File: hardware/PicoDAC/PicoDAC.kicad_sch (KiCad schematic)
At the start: 42 parts, among them CN1 PJ-327A 5JJ, U1 CS43131-CNZR, U2 XIAO-RP2350-DIP, U3 PCA9306DCUR, U4 SN74AXC4T245PWR, U5 XTPS7A2018, U6 TYPEC-955-ARP24, U7 74AHCT1G125GV

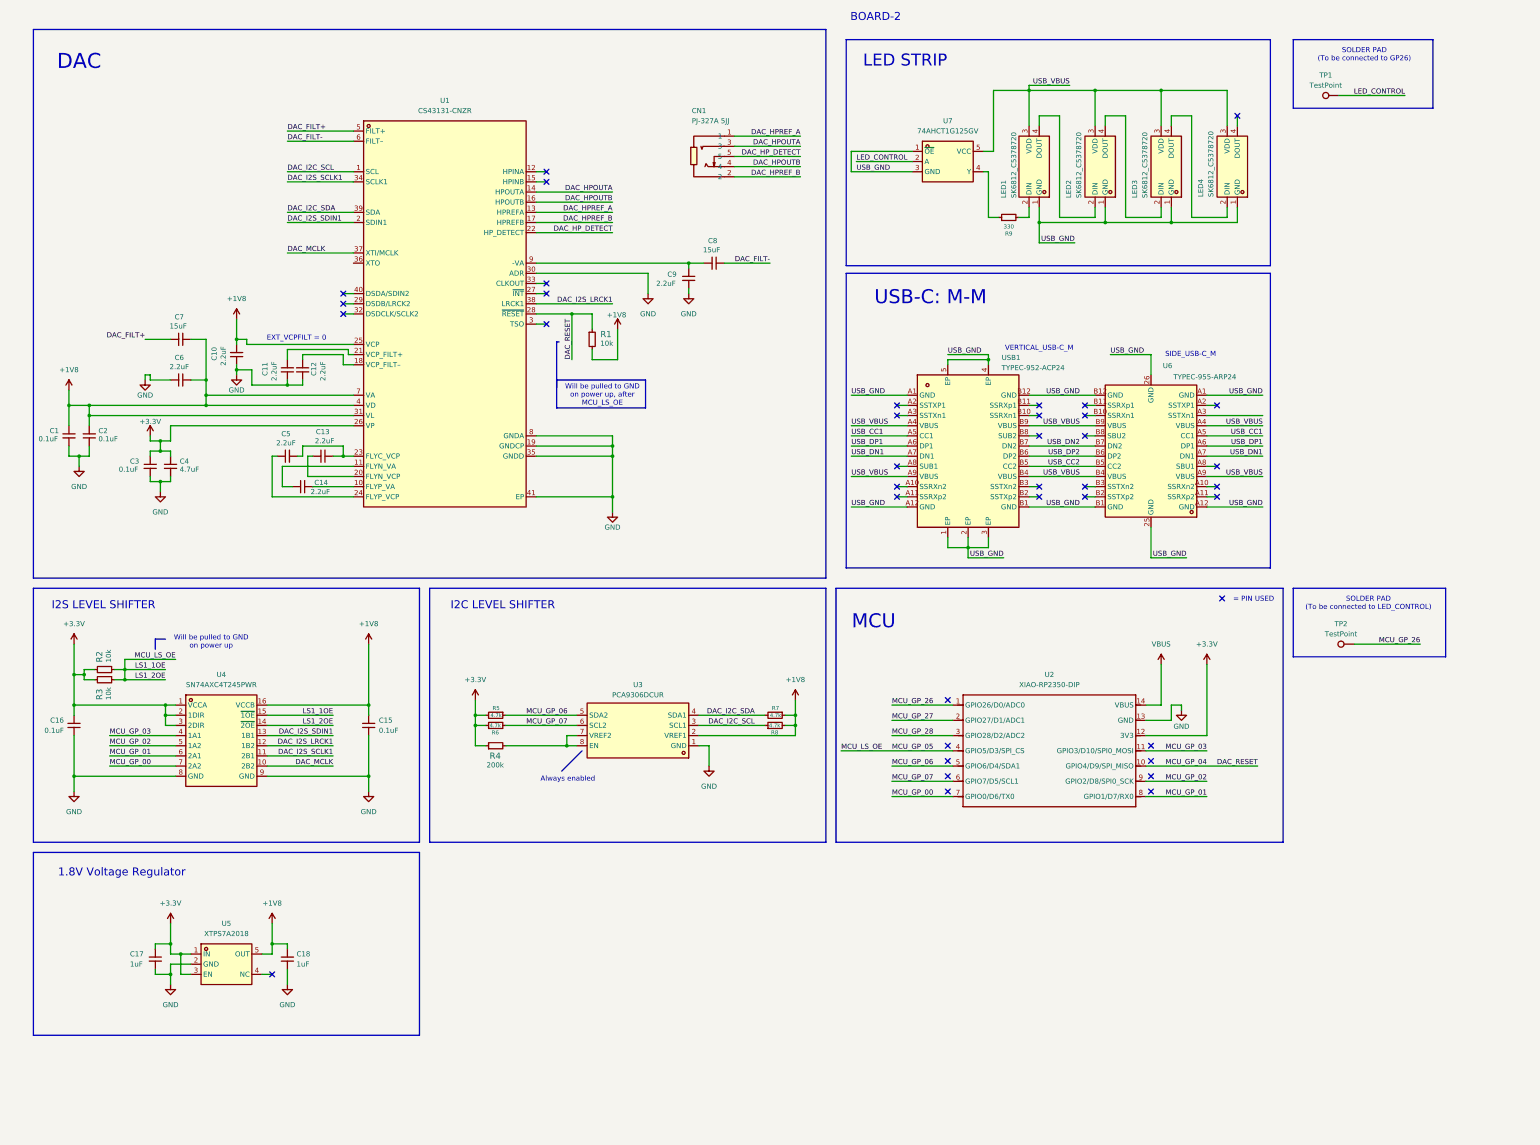
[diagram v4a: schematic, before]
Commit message: update LEDs position, misc changes to PCBs
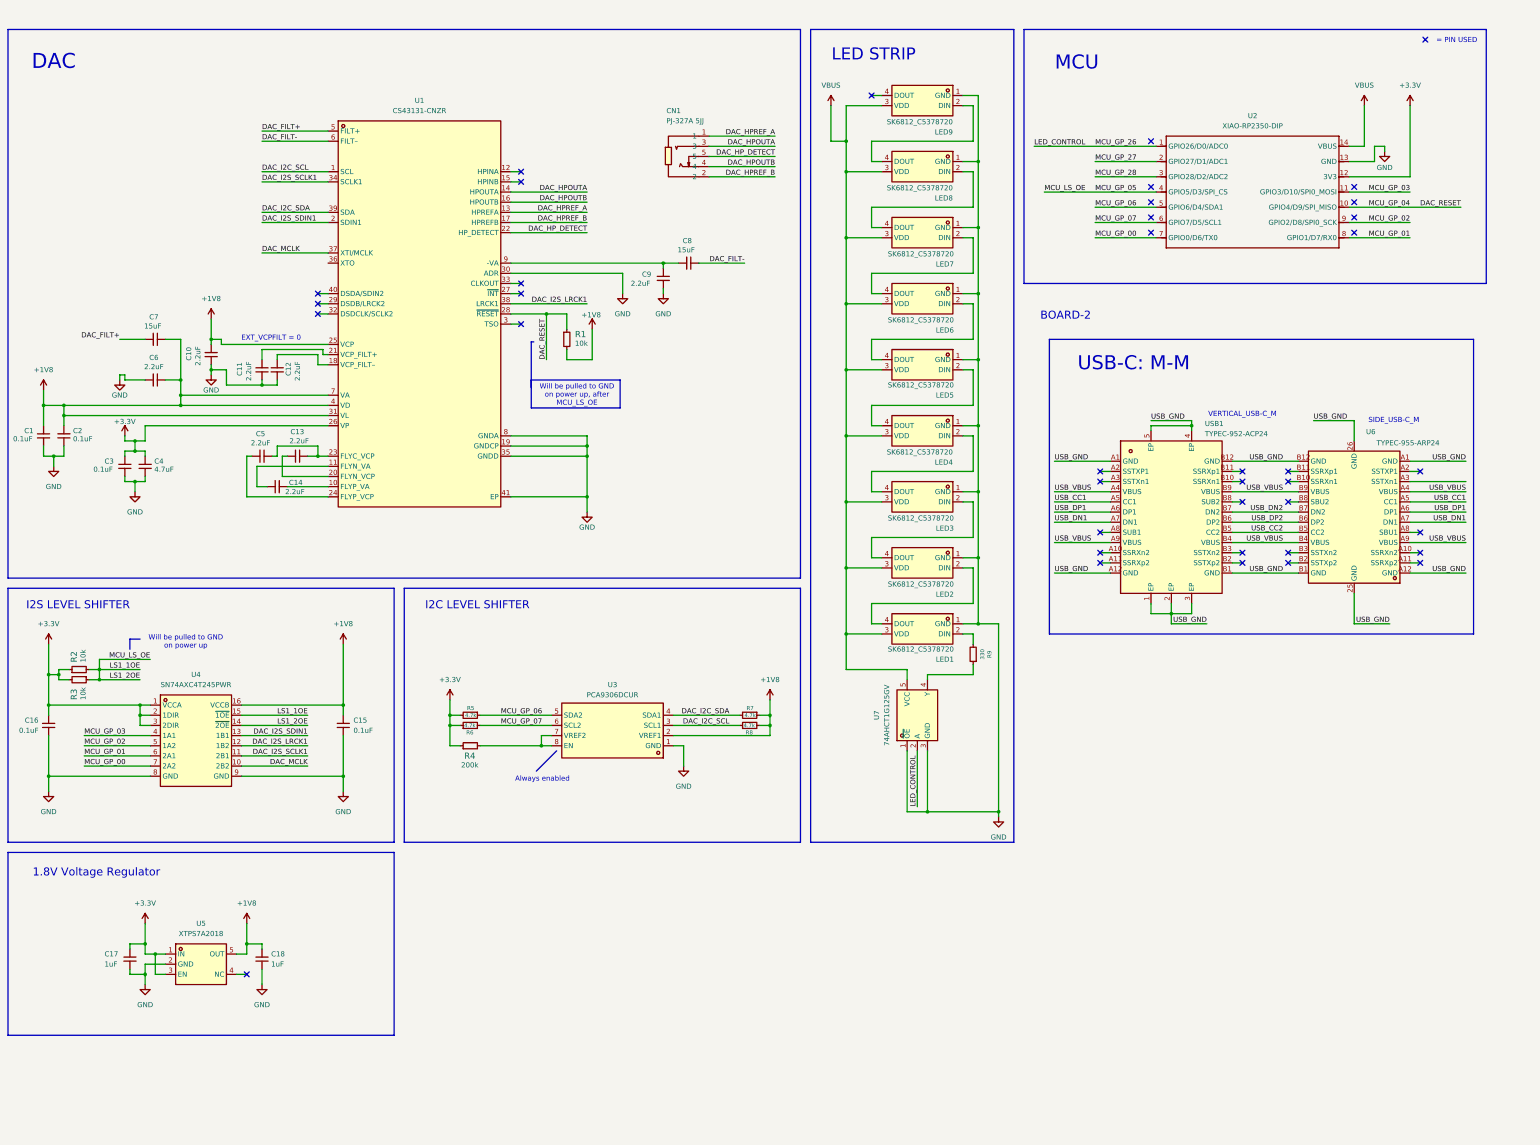
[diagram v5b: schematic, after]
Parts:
- removed TP1, TP2: TestPoint, TestPoint:TestPoint_Pad_D2.0mm, symbol Connector:TestPoint
- added LED5, LED6, LED7, LED8, LED9: SK6812_C5378720, easyeda2kicad:LED-SMD_4P-L5.4-W5.0_SK6812, symbol easyeda2kicad:SK6812_C5378720
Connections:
- net MCU_GP_26 is gone; now on net LED_CONTROL: U2.1 (GPIO26/D0/ADC0)
- net GND: now also LED1.1 (GND), LED2.1 (GND), LED3.1 (GND), LED4.1 (GND), U7.1 (~{OE}), U7.3 (GND), LED5.1 (GND), LED6.1 (GND), LED7.1 (GND), LED8.1 (GND), LED9.1 (GND)
- net USB_GND: no longer LED1.1 (GND), LED2.1 (GND), LED3.1 (GND), LED4.1 (GND), U7.1 (~{OE}), U7.3 (GND)
- net USB_VBUS: no longer LED1.3 (VDD), LED2.3 (VDD), LED3.3 (VDD), LED4.3 (VDD), U7.5 (VCC)
- net VBUS: now also LED1.3 (VDD), LED2.3 (VDD), LED3.3 (VDD), LED4.3 (VDD), U7.5 (VCC), LED5.3 (VDD), LED6.3 (VDD), LED7.3 (VDD), LED8.3 (VDD), LED9.3 (VDD)
- net at LED4.4 (DOUT): now also LED5.2 (DIN)
- new net: LED7.4 (DOUT), LED8.2 (DIN)
- new net: LED8.4 (DOUT), LED9.2 (DIN)
- new net: LED5.4 (DOUT), LED6.2 (DIN)
- new net: LED6.4 (DOUT), LED7.2 (DIN)
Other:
- note removed: "SOLDER PAD (To be connected to GP26)"
- note removed: "SOLDER PAD (To be connected to LED_CONTROL)"
- moved on the sheet: C1, C10, C11, C12, C13, C14, C15, C16, C17, C18, C2, C3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

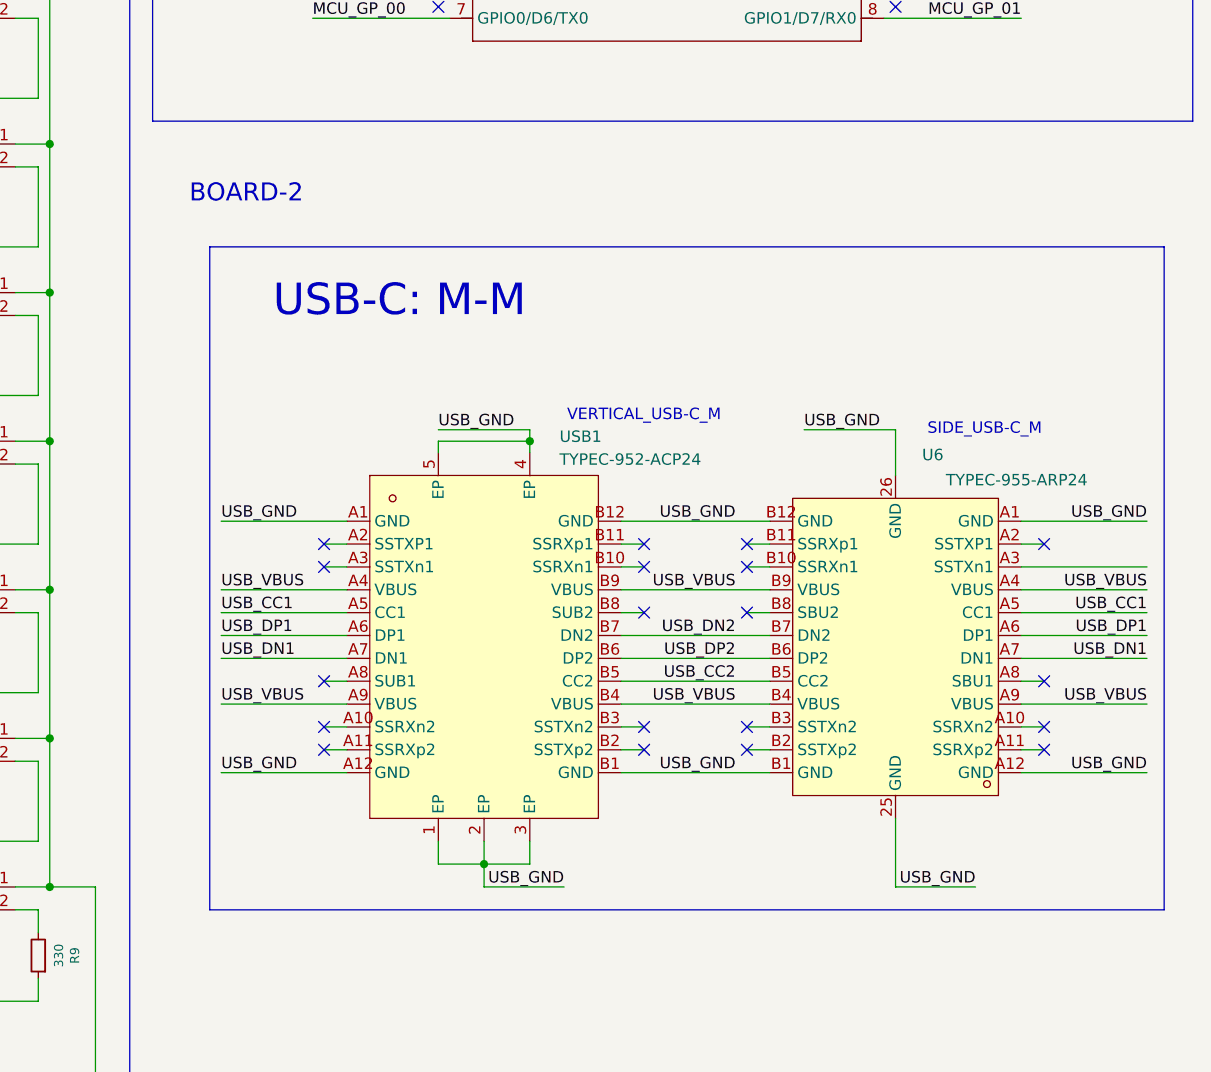
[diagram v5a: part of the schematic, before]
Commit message: moved the LEDs a bit down, repositioned LEDs logic level translator and resistor
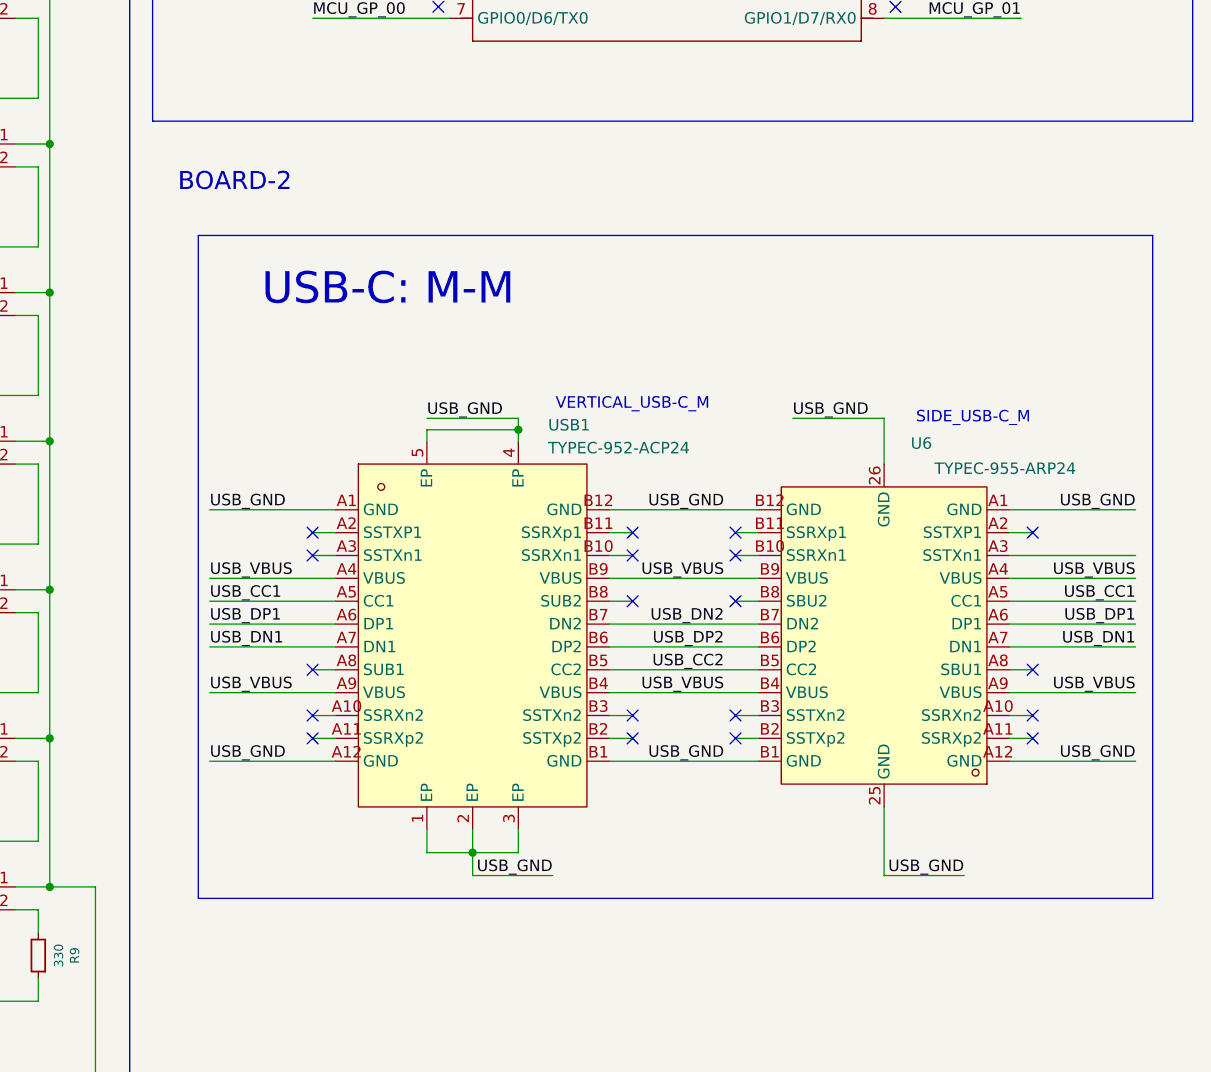
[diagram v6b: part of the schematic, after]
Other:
- moved on the sheet: U6, USB1

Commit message: changed components to get economic assembly
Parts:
- C10, C11, C12, C13, C14, C5, C6, C9: footprint easyeda2kicad:C0201 -> easyeda2kicad:C0402; LCSC Part C335106 -> C170151; MPN GRM033R61A225KE47D -> CL05A225KO5NQNC
- LED1, LED2, LED3, LED4, LED5, LED6, LED7, LED8, LED9: value SK6812_C5378720 -> SK6812_C5142047; footprint easyeda2kicad:LED-SMD_4P-L5.4-W5.0_SK6812 -> easyeda2kicad:LED-SMD_4P-L3.5-W2.8-BR-1; symbol easyeda2kicad:SK6812_C5378720 -> easyeda2kicad:SK6812SMINI-ER; LCSC Part C5378720 -> C5142047; MPN SK6812 -> SK6812SMINI-ER
- U2: now not fitted
- USB6: renamed from U6; value TYPEC-955-ARP24 -> XY-TYPE-C-24PIN-040; footprint easyeda2kicad:USB-C-SMD_TYPE-C-24P-GTJB-040 -> easyeda2kicad:USB-C-SMD_XY-TYPE-C-24PIN-040; symbol easyeda2kicad:TYPE-C24P-GTJB040 -> easyeda2kicad:XY-TYPE-C-24PIN-040; LCSC Part C3151751 -> C53133501; MPN TYPE-C 24P-GTJB 040 -> XY-TYPE-C-24PIN-040; Manufacturer SHOU HAN(首韩) -> XYECONN(辛译)
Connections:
- net USB_GND: now also USB6.15 (EP), USB6.17 (EP); no longer USB6.25 (GND), USB6.26 (GND)
- no-connect marks 39 -> 40
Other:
- moved on the sheet: USB1

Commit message: fixed floating xto pin
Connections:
- net GND: now also U1.36 (XTO)
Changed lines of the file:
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@@
 	(wire
 		(pts
+			(xy 87.63 81.28) (xy 104.14 81.28)
+		)
+		(stroke
+			(width 0)
+			(type default)
+		)
+	)
+	(wire
+		(pts
 			(xy 86.36 137.16) (xy 88.9 137.16)
 		)
@@
 	(wire
 		(pts
+			(xy 87.63 82.55) (xy 87.63 81.28)
+		)
+		(stroke
+			(width 0)
+			(type default)
+		)
+	)
+	(wire
+		(pts
 			(xy 149.86 81.28) (xy 187.96 81.28)
 		)
@@
 					(unit 1)
 				)
+			)
+		)
+	)
+	(symbol
+		(lib_id "power:GND")
+		(at 87.63 82.55 0)
+		(unit 1)
+		(exclude_from_sim no)
+		(in_bom yes)
+		(on_board yes)
+		(dnp no)
+		(fields_autoplaced yes)
+		(property "Reference" "#PWR028"
+			(at 87.63 88.9 0)
+			(effects
+				(font
+					(size 1.27 1.27)
+				)
+				(hide yes)
+			)
+		)
+		(property "Value" "GND"
+			(at 87.63 87.63 0)
+			(effects
+				(font
+					(size 1.27 1.27)
+				)
+			)
+		)
+		(property "Footprint" ""
+			(at 87.63 82.55 0)
+			(effects
+				(font
+					(size 1.27 1.27)
+				)
+				(hide yes)
+			)
+		)
+		(property "Datasheet" ""
+			(at 87.63 82.55 0)
+			(effects
+				(font
+					(size 1.27 1.27)
+				)
+				(hide yes)
+			)
+		)
+		(property "Description" "Power symbol creates a global label with name \"GND\" , ground"
+			(at 87.63 82.55 0)
+			(effects
+				(font
+					(size 1.27 1.27)
+				)
+				(hide yes)
+			)
+		)
+		(pin "1"
+		)
+		(instances
+			(project ""
+				(path "/8ea2595f-0b9c-4299-9b1c-8a8b18638bab"
+					(reference "#PWR028")
+					(unit 1)
+				)
